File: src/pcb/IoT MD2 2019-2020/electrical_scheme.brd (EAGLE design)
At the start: 100 x 80 mm, 12 parts, among them J1 USB3140-XX-XXXX-X-X_REVC, P1 S2B-PH-SM4-TB, Q1 32.768kHz, U1 ATSAMD21E18A-AF, U2 TPS73533DRVT

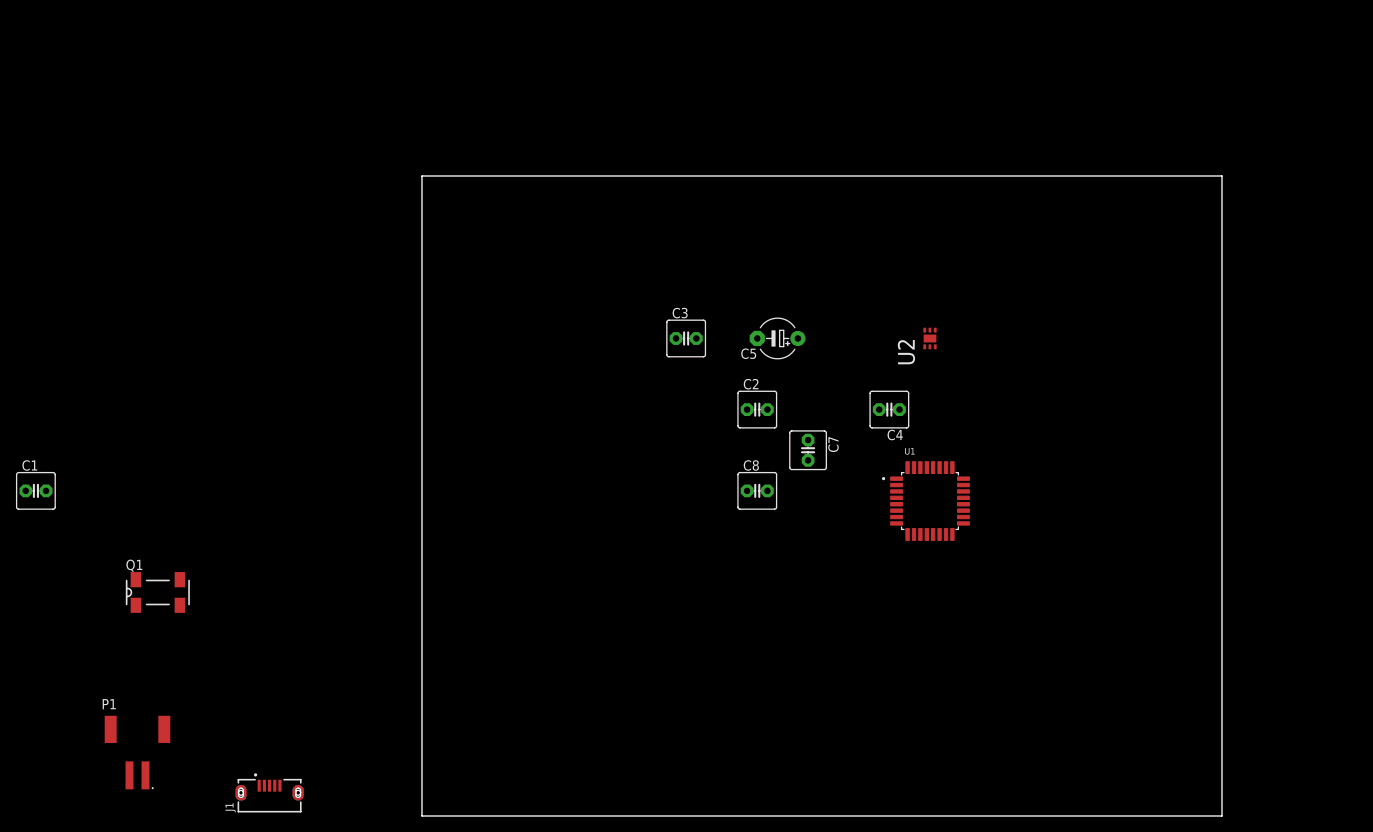
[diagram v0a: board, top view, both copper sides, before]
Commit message: Added board, modified scheme grounds for ground plane
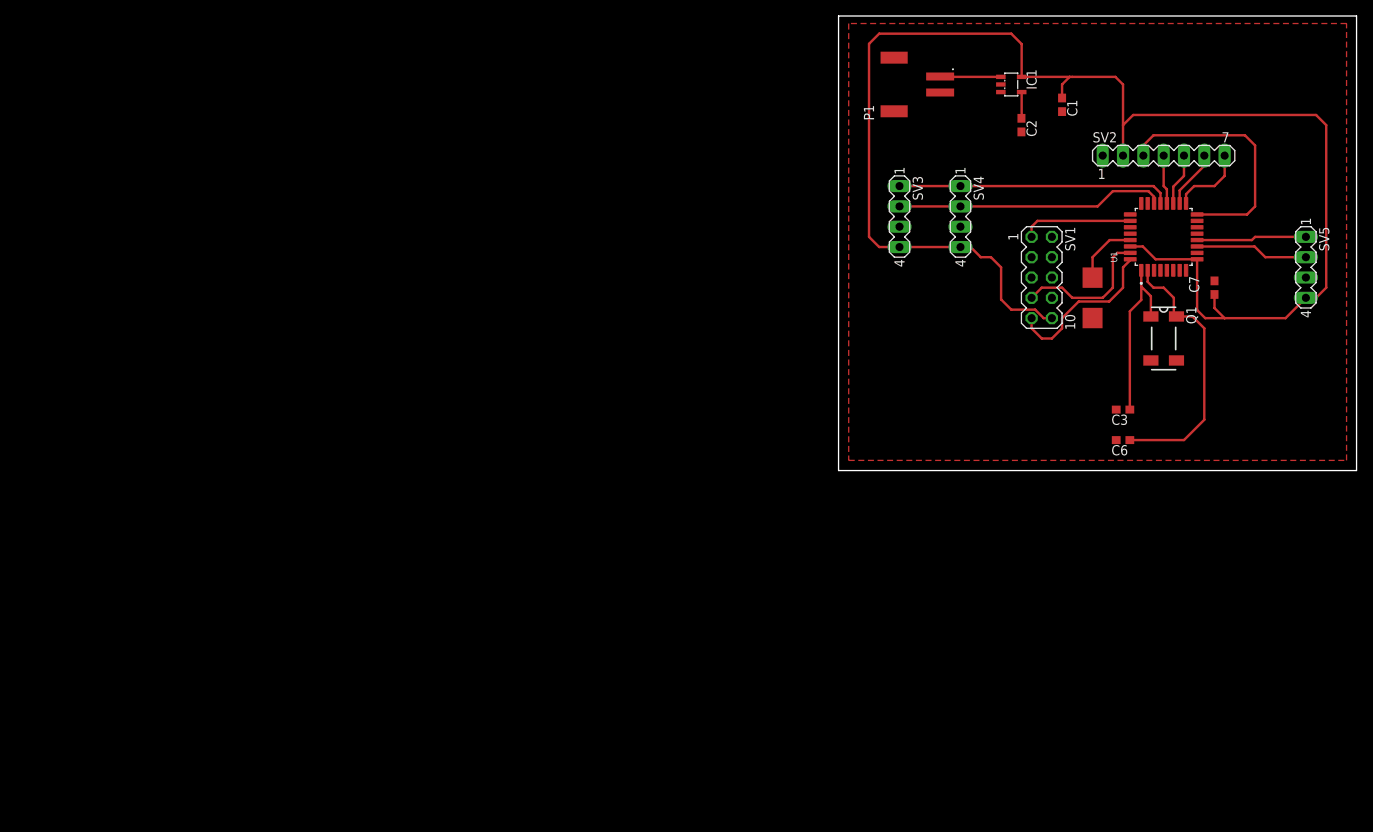
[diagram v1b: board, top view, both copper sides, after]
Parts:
- removed C4: 0.1uF, capacitor-wima:C2.5-5
- removed C5: 1uF, rcl:E5-5
- removed J1: USB3140-XX-XXXX-X-X_REVC, USB3140-XX-XXXX-X-X_REVC:GCT_USB3140-XX-XXXX-X-X_REVC
- removed U2: TPS73533DRVT, TPS73533DRVT:SON65P210X210X80-7N
- added C6: 15pF, rcl:C1608
- added IC1: (no value), v-reg-micrel:SOT23-5
- added SV1: (no value), con-lstb:MA05-2
- added SV2: (no value), con-lstb:MA07-1
- added SV3, SV4, SV5: (no value), con-lstb:MA04-1
- C1: device capacitor-wima:C2.5-5 -> rcl:C1608
- C2: value 1uF -> 470pF; device capacitor-wima:C2.5-5 -> rcl:C1608
- C3: value 0.01uF -> 15pF; device capacitor-wima:C2.5-5 -> rcl:C1608
- C7: value 15pF -> 0.1uF; device capacitor-wima:C2.5-5 -> rcl:C1608
- C8: value 15pF -> 1uF; device capacitor-wima:C2.5-5 -> rcl:C/6032-28R
- moved C1 137.0 mm to (80.0, 88.9), turned to 270 degrees
- moved P1 132.4 mm to (64.8, 91.4), turned to 90 degrees
- moved Q1 129.7 mm to (92.7, 59.7), turned to 270 degrees
- moved C3 55.3 mm to (87.6, 50.8), turned to 180 degrees
- moved C7 54.7 mm to (99.1, 66.0), turned to 90 degrees
- moved C2 48.5 mm to (74.9, 86.4), turned to 270 degrees
- moved C8 48.4 mm to (83.8, 64.8), turned to 90 degrees
- moved U1 44.1 mm to (92.7, 72.4), turned to 90 degrees
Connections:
- removed net 0: C1.2, C2.1, C3.2, C4.2, C5.-, C7.1, C8.1, P1.2, U1.10, U1.28, U2.3
- removed net N$1: C5.+, U1.29
- removed net SWCLK: U1.31
- removed net VBUS: J1.1
- new net MISO: SV2.4, U1.20
- new net MOSI: SV2.7, U1.17
- new net NSS: SV2.5, U1.19
- new net RESET: SV1.1, U1.26
- new net RESET_LORA: SV2.3, U1.16
- new net RX: SV5.2, U1.11
- new net SCK: SV2.6, U1.18
- new net SCL: SV3.2, SV4.2, U1.22
- new net SDA: SV3.1, SV4.1, U1.21
- new net SWDCLK: SV1.7, U1.31
- new net TX: SV5.1, U1.12
- new net VDDCORE: C8.+, U1.29
- net GND: now also C1.2, C2.2, C3.2, C6.2, C7.2, C8.-, IC1.2, P1.2, SV1.6, SV1.8, SV2.1, SV3.3, SV4.3, SV5.3, U1.10, U1.28; no longer J1.5
- net N$2: now also IC1.1, IC1.3; no longer C2.2, U2.4, U2.6
- net N$3: now also C2.1, IC1.4; no longer C3.1, U2.2
- net N$4: now also C3.1, Q1.1; no longer C7.2, Q1.4
- net N$5: now also C6.1, Q1.4; no longer C8.2, Q1.1
- net SWDIO: now also SV1.9
- net VDD: now also C7.1, IC1.5, SV1.10, SV2.2, SV3.4, SV4.4, SV5.4; no longer C4.1, U2.1
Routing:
- net VDD: track 0.00 -> 186.5 mm
- net SDA: track 0.00 -> 34.3 mm
- net N$5: track 0.00 -> 33.9 mm
- net SCL: track 0.00 -> 33.7 mm
- net RESET_LORA: track 0.00 -> 31.6 mm
- net N$4: track 0.00 -> 22.2 mm
- net SWDIO: track 0.00 -> 20.5 mm
- net SWDCLK: track 0.00 -> 17.9 mm
- net RX: track 0.00 -> 14.2 mm
- net RESET: track 0.00 -> 13.9 mm
- net TX: track 0.00 -> 13.8 mm
- net MOSI: track 0.00 -> 9.46 mm
- net VDDCORE: track 0.00 -> 8.15 mm
- net N$2: track 0.00 -> 7.83 mm
- net SCK: track 0.00 -> 7.26 mm
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- added copper zone on layer 1, net GND
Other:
- board size 100 x 80 mm -> 64.8 x 56.8 mm
